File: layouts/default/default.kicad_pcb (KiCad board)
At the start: 2 copper layers, 38 x 75 mm, 43 parts, among them U2 LDO Vin max Iq, U3 LDO Vin max Iq

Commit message: Update layout
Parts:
- added C10: 100nF ±10% 16V X7R, atopile:C0402-b3ef17, B.Cu at (1.50, 15.2)
- added C11: 100nF ±10% 16V X7R, atopile:C0402-b3ef17, B.Cu at (1.50, 21.2)
- added C12: 100nF ±10% 16V X7R, atopile:C0402-b3ef17, B.Cu at (1.50, 27.2)
- added C17: , atopile:C_0402_1005Metric, B.Cu at (-0.95, 26.4)
- added C8: 100nF ±10% 16V X7R, atopile:C0402-b3ef17, B.Cu at (1.50, 3.00)
- added C9: 100nF ±10% 16V X7R, atopile:C0402-b3ef17, B.Cu at (1.50, 9.00)
- added S1: , atopile:KEY-SMD_4P-L4.2-W3.2-P2.20-LS4.6-a2ccf0, F.Cu at (7.07, 23.1)
- added S2: , atopile:KEY-SMD_4P-L4.2-W3.2-P2.20-LS4.6-a2ccf0, F.Cu at (7.07, 3.10)
- added XTAL1: , atopile:CRYSTAL-SMD_L3.2-W1.5-1-214bf9, F.Cu at (-11.0, 13.0)
- LED1, LED2, LED3, LED4, LED5, U7: moved to B.Cu
- moved U2 431.1 mm to (-21.0, -12.0)
- moved C7 277.4 mm to (2.50, 68.5), turned to 90 degrees
- moved X1 241.5 mm to (16.0, 12.0), turned to 90 degrees
- moved R1 205.2 mm to (-5.00, -13.0)
- moved R11 202.6 mm to (1.25, 68.5), turned to 90 degrees
- moved U7 176.7 mm to (16.2, 61.5)
- moved U3 174.1 mm to (-14.0, -12.0)
- moved R10 149.3 mm to (0.00, 68.5), turned to 90 degrees
- moved R9 109.6 mm to (-1.25, 68.5), turned to 90 degrees
- moved U1 42.4 mm to (3.00, 9.50)
- moved R2 37.5 mm to (3.00, -11.0)
- moved R5 22.0 mm to (-14.0, 16.0), turned to 90 degrees
- moved R7 16.5 mm to (13.0, 10.0)
- moved U8 14.0 mm to (-1.50, 19.0)
- moved J2 13.4 mm to (13.1, 21.8), turned to 180 degrees
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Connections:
- C1 pad 1: hv -> hv-2
- C1 pad 2: gnd-1 -> gnd
- C3 pad 1: hv-3 -> hv
- C3 pad 2: gnd-1 -> gnd
- C4 pad 2: gnd-1 -> gnd
- C5 pad 2: gnd-1 -> gnd
- C7 pad 2: gnd-1 -> gnd
- J1 pad 1: gnd-1 -> gnd
- J1 pad 10: line-9 -> line-4
- J1 pad 11: line-6 -> line-3
- J1 pad 13: usb_psu-hv -> hv-1
- J1 pad 14: gnd-1 -> gnd
- J1 pad 2: usb_psu-hv -> hv-1
- J1 pad 3: line-9 -> line-4
- J1 pad 4: line-6 -> line-3
- J1 pad 6: usb_psu-hv -> hv-1
- J1 pad 7: gnd-1 -> gnd
- J1 pad 8: gnd-1 -> gnd
- J1 pad 9: usb_psu-hv -> hv-1
- J2 pad 1: vindriktning_interface-line-1 -> vindriktning_interface-line
- J2 pad 2: vindriktning_interface-line -> vindriktning_interface-line-1
- J2 pad 3: hv-1 -> hv-3
- J2 pad 4: gnd-1 -> gnd
- LED1 pad 1: gnd-1 -> gnd
- LED1 pad 2: led_string-line-1 -> led_string-line-3
- LED1 pad 3: hv-1 -> hv-3
- LED2 pad 1: gnd-1 -> gnd
- LED2 pad 3: hv-1 -> hv-3
- LED2 pad 4: led_string-line-3 -> led_string-line-2
- LED3 pad 1: gnd-1 -> gnd
- LED3 pad 2: led_string-line-3 -> led_string-line-2
- LED3 pad 3: hv-1 -> hv-3
- LED4 pad 1: gnd-1 -> gnd
- LED4 pad 3: hv-1 -> hv-3
- LED4 pad 4: led_string-line-2 -> led_string-line-1
- LED5 pad 1: gnd-1 -> gnd
- LED5 pad 2: led_string-line-2 -> led_string-line-1
- LED5 pad 3: hv-1 -> hv-3
- Q1 pad 1: line -> line-6
- R1 pad 1: line-3 -> line-8
- R1 pad 2: hv -> hv-2
- R10 pad 2: gnd-1 -> gnd
- R11 pad 2: gnd-1 -> gnd
- R12 pad 1: line -> line-6
- R12 pad 2: gnd-1 -> gnd
- R2 pad 1: line-4 -> line-5
- R2 pad 2: hv -> hv-2
- R4 pad 2: hv-3 -> hv
- R6 pad 1: line-3 -> line-8
- R6 pad 2: hv-3 -> hv
- R7 pad 1: line-2 -> line-9
- R7 pad 2: hv-3 -> hv
- R9 pad 2: gnd-1 -> gnd
- U1 pad 10: line-4 -> line-5
- U1 pad 19: hv -> hv-2
- U1 pad 20: gnd-1 -> gnd
- U1 pad 21: gnd-1 -> gnd
- U1 pad 6: gnd-1 -> gnd
- U1 pad 7: hv -> hv-2
- U1 pad 9: line-3 -> line-8
- U2 pad 1: hv-1 -> hv-3
- U2 pad 2: gnd-1 -> gnd
- U2 pad 3: hv-1 -> hv-3
- U2 pad 5: hv-3 -> hv
- U3 pad 1: hv-1 -> hv-3
- U3 pad 2: gnd-1 -> gnd
- U3 pad 3: hv-1 -> hv-3
- U3 pad 5: hv -> hv-2
- U4 pad 1: hv -> hv-2
- U4 pad 3: gnd-1 -> gnd
- U4 pad 4: line-4 -> line-5
- U4 pad 6: line-3 -> line-8
- U5 pad 1: gnd-1 -> gnd
- U5 pad 11: gnd-1 -> gnd
- U5 pad 14: gnd-1 -> gnd
- U5 pad 16: mcu.mcu.esp32_c3_mini_1.ic-line-1 -> mcu.mcu.esp32_c3_mini_1.ic-line
- U5 pad 18: line -> line-6
- U5 pad 2: gnd-1 -> gnd
- U5 pad 20: line-8 -> line-10
- U5 pad 21: mcu.mcu.esp32_c3_mini_1.ic-line -> mcu.mcu.esp32_c3_mini_1.ic-line-1
- U5 pad 22: line-2 -> line-9
- U5 pad 26: line-9 -> line-4
- U5 pad 27: line-6 -> line-3
- U5 pad 3: hv-3 -> hv
- U5 pad 30: line-5 -> line
- U5 pad 31: line-10 -> line-2
- U5 pad 36: gnd-1 -> gnd
- U5 pad 37: gnd-1 -> gnd
- U5 pad 38: gnd-1 -> gnd
- U5 pad 39: gnd-1 -> gnd
- U5 pad 40: gnd-1 -> gnd
- U5 pad 41: gnd-1 -> gnd
- U5 pad 42: gnd-1 -> gnd
- U5 pad 43: gnd-1 -> gnd
- U5 pad 44: gnd-1 -> gnd
- U5 pad 45: gnd-1 -> gnd
- U5 pad 46: gnd-1 -> gnd
- U5 pad 47: gnd-1 -> gnd
- U5 pad 48: gnd-1 -> gnd
- U5 pad 49: gnd-1 -> gnd
- U5 pad 5: line-3 -> line-8
- U5 pad 50: gnd-1 -> gnd
- U5 pad 51: gnd-1 -> gnd
- U5 pad 52: gnd-1 -> gnd
- U5 pad 53: gnd-1 -> gnd
- U5 pad 54: gnd-1 -> gnd
- U5 pad 55: gnd-1 -> gnd
- U5 pad 56: gnd-1 -> gnd
- U5 pad 57: gnd-1 -> gnd
- U5 pad 58: gnd-1 -> gnd
- U5 pad 59: gnd-1 -> gnd
- U5 pad 6: line-4 -> line-5
- U5 pad 60: gnd-1 -> gnd
- U5 pad 61: gnd-1 -> gnd
- U6 pad 1: vindriktning_interface-line -> vindriktning_interface-line-1
- U6 pad 2: gnd-1 -> gnd
- U6 pad 3: hv -> hv-2
- U6 pad 5: line-2 -> line-9
- U6 pad 6: hv -> hv-2
- U6 pad 7: hv-1 -> hv-3
- U6 pad 8: vindriktning_interface-line-1 -> vindriktning_interface-line
- U7 pad 1: line-8 -> line-10
- U7 pad 2: line-10 -> line-2
- U7 pad 3: line-5 -> line
- U7 pad 4: gnd-1 -> gnd
- U7 pad 5: hv-1 -> hv-3
- U8 pad 2: gnd-1 -> gnd
- U8 pad 3: hv -> hv-2
- U8 pad 6: hv -> hv-2
- U8 pad 7: hv-1 -> hv-3
- U8 pad 8: led_string-line-1 -> led_string-line-3
- X1 pad 1: gnd -> gnd-1
- X1 pad 2: hv-2 -> hv-4
- X1 pad 3: line-4 -> line-5
- X1 pad 4: line-3 -> line-8
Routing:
- net (no net): track 0.00 -> 38.0 mm
- net gnd: track 0.00 -> 36.7 mm
- net hv-3: track 0.00 -> 31.4 mm, vias 0 -> 4
- net led_string-line-4: track 6.99 -> 38.0 mm
- net vindriktning_interface-line: track 0.00 -> 22.3 mm
- net vindriktning_interface-line-1: track 0.00 -> 18.7 mm
- net hv-4: track 0.00 -> 11.4 mm
- net mount[1]: track 0.00 -> 10.9 mm
- net led_string.leds[4]-line: track 0.00 -> 9.81 mm
- net co2_sensor.footprint.pins[19].net-net: track 0.00 -> 9.81 mm
- net cc1: track 0.00 -> 9.81 mm
- net mcu.mcu.low_speed_crystal_clock-net: track 0.00 -> 7.26 mm
- net mcu.mcu-line-1: track 0.00 -> 7.26 mm
- net led_string-line-1: track 2.77 -> 9.81 mm
- net led_string-line-3: track 6.99 -> 0.00 mm
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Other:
- board text added: "325bd98"

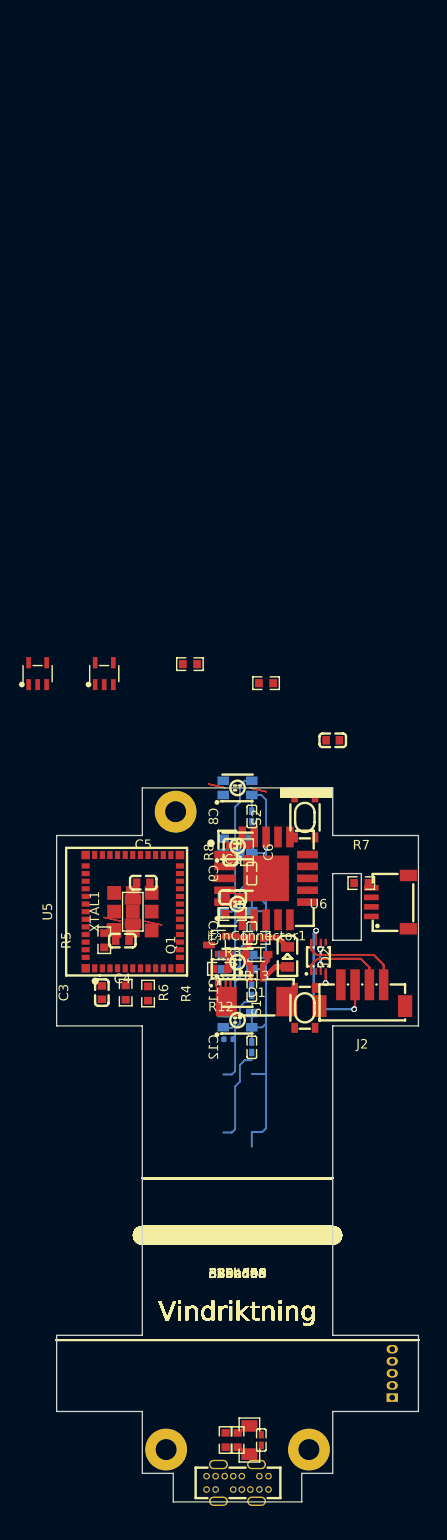
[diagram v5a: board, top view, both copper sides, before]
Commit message: Make it build with ato 0.8.x
- refactor modules
- clean up modules and structure
- convert some from fabll to ato
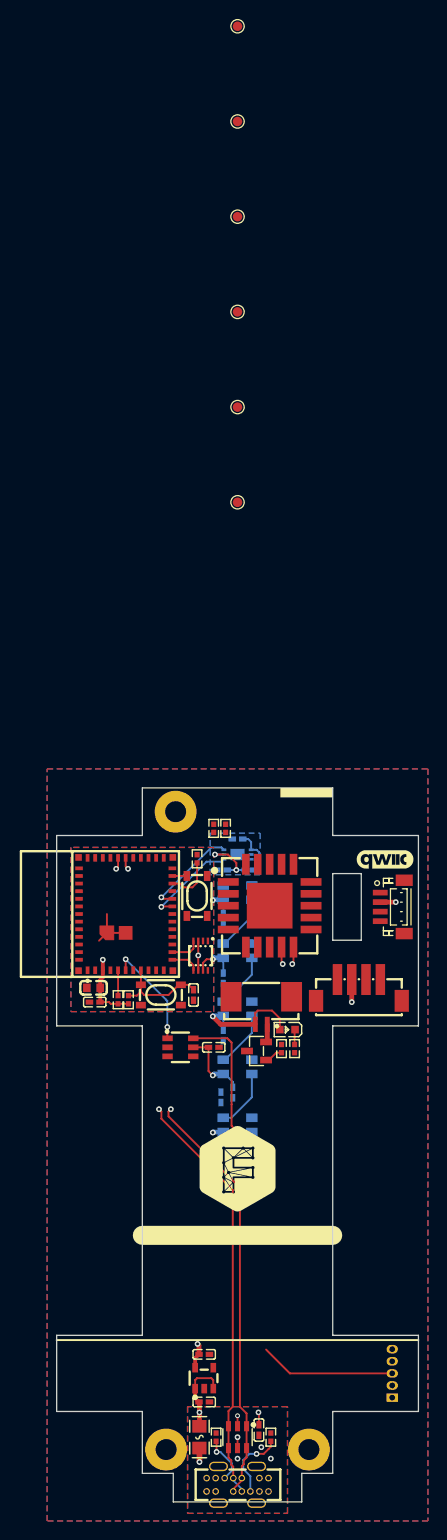
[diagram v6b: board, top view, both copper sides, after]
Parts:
- removed C17: , atopile:C_0402_1005Metric
- removed D1: 450mV, atopile:SOD-323_L1.8-W1.3-LS2.5-RD-b55baa
- removed D2: , atopile:LED0805-R-RD-d1137b
- removed J1: , atopile:USB-C-TH_TYPE-C-USB-14P-1a34cb
- removed R13, R7, R8: 10kΩ ±1% 100mW, atopile:R0603-ebcab9
- removed S1, S2: , atopile:KEY-SMD_4P-L4.2-W3.2-P2.20-LS4.6-a2ccf0
- removed XTAL1: , atopile:CRYSTAL-SMD_L3.2-W1.5-1-214bf9
- added C13: 100nF ±10% 16V X7R, atopile:C0402-b3ef17, B.Cu at (-1.62, 8.62)
- added C14: 100nF ±10% 16V X7R, atopile:C0402-b3ef17, F.Cu at (2.25, 67.5)
- added CN1: , atopile:CONN-SMD_BM04B-SRSS-TB-6963ef, F.Cu at (16.2, 12.5)
- added LOGO1: , lib:faebrykLogo_8x9mm, F.Cu at (0.00, 40.0)
- added TP1: , TestPoint:TestPoint_Pad_D1.0mm, F.Cu at (0.00, -70.0)
- added TP2: , TestPoint:TestPoint_Pad_D1.0mm, F.Cu at (0.00, -30.0)
- added TP3: , TestPoint:TestPoint_Pad_D1.0mm, F.Cu at (0.00, -50.0)
- added TP4: , TestPoint:TestPoint_Pad_D1.0mm, F.Cu at (0.00, -80.0)
- added TP5: , TestPoint:TestPoint_Pad_D1.0mm, F.Cu at (0.00, -40.0)
- added TP6: , TestPoint:TestPoint_Pad_D1.0mm, F.Cu at (0.00, -60.0)
- added U10: , atopile:VSON8_L2.0-W2.3-P0.50-LS3.1-BL-9e6526, F.Cu at (-3.88, 17.6)
- added U11: 2V, lib:LED0603-RD, F.Cu at (5.25, 25.4)
- added U12: , atopile:SOT-23-6_L2.9-W1.6-P0.95-LS2.8-BL-d2c740, F.Cu at (0.00, 68.2)
- added U13: , atopile:F0805-d5954a, F.Cu at (-4.00, 68.2)
- added U9: , lib:qwiic_6mm, F.Cu at (15.5, 7.50)
- C1, C2: value 100nF ±10% 50V X7R -> 100nF ±10% 16V X7R; footprint atopile:C0603-bd72f6 -> atopile:C0402-b3ef17
- C10: value 100nF ±10% 16V X7R -> 22µF ±20% 6.3V X5R; footprint atopile:C0402-b3ef17 -> atopile:C0603-bd72f6; moved to F.Cu
- C11: moved to F.Cu
- C12: value 100nF ±10% 16V X7R -> 1µF ±10% 16V X5R; moved to F.Cu
- C3: value 1µF ±10% 50V X5R -> 100nF ±10% 16V X7R; footprint atopile:C0603-bd72f6 -> atopile:C0402-b3ef17
- C4, C5, C6: value 100nF ±10% 50V X7R -> 100nF ±10% 16V X7R; footprint atopile:C0603-bd72f6 -> atopile:C0402-b3ef17; moved to B.Cu
- C7: value 100nF ±5% 16V X7R -> 100nF ±10% 16V X7R; moved to B.Cu
- Q1: footprint atopile:SOT-23-3_L2.9-W1.3-P1.90-LS2.4-BL-1-fcaf94 -> atopile:SOT-23-3_L2.9-W1.3-P1.90-LS2.4-BR-688f29
- R1: value 10kΩ ±1% 100mW -> 1kΩ ±1% 62.5mW; footprint atopile:R0603-ebcab9 -> atopile:R0402-56259e; moved to B.Cu
- R10: value 5.1kΩ ±1% 100mW -> 1kΩ ±1% 62.5mW; footprint atopile:R0603-ebcab9 -> atopile:R0402-56259e
- R11: value 1MΩ ±1% 250mW -> 10kΩ ±1% 62.5mW; footprint atopile:R1206-bdb864 -> atopile:R0402-56259e
- R12, R3, R4, R5: value 10kΩ ±1% 100mW -> 10kΩ ±1% 62.5mW; footprint atopile:R0603-ebcab9 -> atopile:R0402-56259e
- R2, R6: value 10kΩ ±1% 100mW -> 5.1kΩ ±1% 62.5mW; footprint atopile:R0603-ebcab9 -> atopile:R0402-56259e
- R9: value 5.1kΩ ±1% 100mW -> 10kΩ ±1% 62.5mW; footprint atopile:R0603-ebcab9 -> atopile:R0402-56259e
- U2: value LDO Vin max Iq -> LDO 3.3V ±0% 850.5mA 320mV Vin max Iq 10µA; footprint atopile:SOT-23-5_L3.0-W1.7-P0.95-LS2.8-BL-01dfeb -> atopile:SOT-23-5_L2.9-W1.6-P0.95-LS2.8-BR-2dcca4
- U3: value LDO Vin max Iq -> (none); footprint atopile:SOT-23-5_L3.0-W1.7-P0.95-LS2.8-BL-01dfeb -> atopile:SOT-23-6_L2.9-W1.6-P0.95-LS2.8-BR-bfc73b
- U5: footprint atopile:WIFIM-SMD_ESP32-C3-MINI-MINI-1U-1cb675 -> lib:KEY-SMD_4P-L4.2-W3.2-P2.20-LS4.6
- U6: footprint atopile:VSON8_L2.0-W2.3-P0.50-LS3.1-BL-9e6526 -> atopile:WIFIM-SMD_ESP32-C3-MINI-1-fcb454
- U7: footprint atopile:SENSORM-TH_HLK-LD2410B-P-2a325e -> lib:KEY-SMD_4P-L4.2-W3.2-P2.20-LS4.6; moved to F.Cu
- U8: footprint atopile:VSON8_L2.0-W2.3-P0.50-LS3.1-BL-9e6526 -> atopile:SENSORM-TH_HLK-LD2410B-P-2a325e; moved to B.Cu
- X1: footprint atopile:CONN-SMD_4P-P1.00_SM04B-SRSS-TB-LF-SN-d36980 -> atopile:USB-C-TH_TYPE-C-USB-14P-1a34cb
- moved R2 79.4 mm to (-2.25, 68.2), turned to 90 degrees
- moved U2 76.0 mm to (-3.50, 62.0), turned to -90 degrees
- moved C1 70.8 mm to (-3.50, 64.5)
- moved R11 64.3 mm to (-1.25, 4.25)
- moved X1 63.3 mm to (0.00, 73.2), turned to 0 degrees
- moved R6 49.1 mm to (3.50, 68.2), turned to 90 degrees
- moved C7 48.7 mm to (-1.50, 20.0), turned to -90 degrees
- moved C2 48.1 mm to (-3.50, 59.5)
- moved U7 46.6 mm to (-8.05, 21.8), turned to 180 degrees
- moved U8 46.1 mm to (16.2, 61.5)
- moved R10 41.5 mm to (6.00, 27.4), turned to -90 degrees
- moved R9 41.5 mm to (4.62, 27.4)
- moved U3 40.1 mm to (-6.00, 27.2), turned to 180 degrees
- moved LED1 35.4 mm to (0.00, 35.4), turned to 0 degrees
- moved C5 24.0 mm to (-0.50, 32.0), turned to -90 degrees
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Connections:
- net ldo_mcu.footprint.pins[3].net-net renamed ldo.ldo.footprint.pins[3].net-net
- net ldo_peripheral.footprint.pins[3].net-net renamed led_buffer-line-1
- net led_string-line renamed line-19
- net led_string-line-2 renamed line-13
- C10 pad 1: hv-3 -> hv
- C11 pad 1: hv-3 -> hv
- C12 pad 1: hv-3 -> output
- C2 pad 1: mcu.mcu.boot_switch.lp_filter-line -> hv
- C2 pad 2: mcu.mcu.boot_switch.lp_filter-gnd -> gnd
- C3 pad 1: hv -> hv-2
- C4 pad 1: mcu.mcu.low_speed_crystal_clock-net -> hv-2
- C5 pad 1: mcu.mcu-line-1 -> hv-2
- C6 pad 1: mcu.mcu.reset_switch.lp_filter-line -> hv-2
- C6 pad 2: mcu.mcu.reset_switch.lp_filter-gnd -> gnd
- C7 pad 1: shield -> hv-2
- C8 pad 1: hv-3 -> hv-2
- C9 pad 1: hv-3 -> hv
- FanConnector1 pad 1: vindriktning_interface.fan_controller-gnd-1 -> vindriktning_interface.fan_controller-gnd
- FanConnector1 pad 2: vindriktning_interface.fan_controller-hv -> hv-2
- H1 pad 1: (no net) -> pcb_mount.screw_holes[0]-contact
- H2 pad 1: (no net) -> pcb_mount.screw_holes[1]-contact
- H3 pad 1: (no net) -> pcb_mount.screw_holes[2]-contact
- J2 pad 1: vindriktning_interface-line -> pin[0]
- J2 pad 2: vindriktning_interface-line-1 -> pin[1]
- J2 pad 3: hv-3 -> hv-2
- LED1 pad 2: led_string-line-3 -> line-21
- LED1 pad 3: hv-3 -> hv-2
- LED2 pad 3: hv-3 -> hv-2
- LED3 pad 3: hv-3 -> hv-2
- LED3 pad 4: led_string-line-4 -> line-3
- LED4 pad 2: led_string-line-4 -> line-3
- LED4 pad 3: hv-3 -> hv-2
- LED4 pad 4: led_string-line-1 -> line-2
- LED5 pad 2: led_string-line-1 -> line-2
- LED5 pad 3: hv-3 -> hv-2
- LED5 pad 4: led_string.leds[4]-line -> line
- Q1 pad 1: line-6 -> line-16
- Q1 pad 2: vindriktning_interface.fan_controller-gnd-1 -> vindriktning_interface.fan_controller-gnd
- Q1 pad 3: vindriktning_interface.fan_controller-gnd -> gnd
- R1 pad 1: line-8 -> hv
- R1 pad 2: hv-2 -> DVI
- R10 pad 1: cc2 -> cathode
- R10 pad 2: gnd -> vindriktning_interface.fan_controller-gnd
- R11 pad 1: shield -> line-5
- R11 pad 2: gnd -> hv
- R12 pad 2: gnd -> hv
- R2 pad 1: line-5 -> line-12
- R2 pad 2: hv-2 -> gnd
- R3 pad 1: mcu.mcu.boot_switch-line -> line-4
- R3 pad 2: mcu.mcu.boot_switch.lp_filter-line -> hv
- R4 pad 1: mcu.mcu-line -> line-14
- R5 pad 1: mcu.mcu.low_speed_crystal_clock-net -> hv
- R5 pad 2: mcu.mcu-line-2 -> output
- R6 pad 1: line-8 -> line-15
- R6 pad 2: hv -> gnd
- R9 pad 1: cc1 -> line-16
- U1 pad 10: line-5 -> line-6
- U1 pad 19: hv-2 -> hv
- U1 pad 7: hv-2 -> hv
- U1 pad 9: line-8 -> line-5
- U2 pad 1: hv-3 -> hv-2
- U2 pad 3: hv-3 -> hv-2
- U3 pad 1: hv-3 -> line-7
- U3 pad 3: hv-3 -> led_buffer-line
- U4 pad 1: hv-2 -> hv
- U4 pad 2: lux_sensor.ic-line-1 -> gnd
- U4 pad 4: line-5 -> line-6
- U4 pad 5: lux_sensor.ic-line -> DVI
- U4 pad 6: line-8 -> line-5
- U4 pad 7: lux_sensor.ic-line-2 -> gnd
- U5 pad 3: hv -> output-1
- U5 pad 4: mcu.mcu.esp32_c3_mini_1.ic.footprint.pins[33].net-net -> output-1
- U6 pad 1: vindriktning_interface-line-1 -> gnd
- U6 pad 3: hv-2 -> hv
- U6 pad 4: line-1 -> mcu.ic.footprint.pins[33].net-net
- U6 pad 5: line-9 -> line-4
- U6 pad 6: hv-2 -> line-7
- U6 pad 7: hv-3 -> mcu.ic.footprint.pins[50].net-net
- U6 pad 8: vindriktning_interface-line -> output
- U7 pad 1: line-10 -> gnd
- U7 pad 2: line-2 -> gnd
- U7 pad 3: line -> output
- U7 pad 4: gnd -> output
- U8 pad 1: led_string.runtime_anon[0]-line-1 -> line-10
- U8 pad 2: gnd -> line-18
- U8 pad 3: hv-2 -> line-20
- U8 pad 4: led_string.runtime_anon[0]-line -> gnd
- U8 pad 5: line-7 -> hv-2
- X1 pad 1: gnd-1 -> gnd
- X1 pad 2: hv-4 -> hv-1
- X1 pad 3: line-5 -> line-17
- X1 pad 4: line-8 -> line-1
- X1 pad 5: qwiic_connector.footprint.pins[4].net-net -> line-15
- X1 pad 6: qwiic_connector.footprint.pins[5].net-net -> hv-1
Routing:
- net line-17: track 0.00 -> 44.2 mm, vias 0 -> 1
- net line-1: track 2.41 -> 44.1 mm, vias 2 -> 1
- net led_string-line-4: track 38.0 -> 0.00 mm
- net (no net): track 38.0 -> 0.00 mm
- net hv-2: track 6.28 -> 41.9 mm, vias 4 -> 9
- net hv-3: track 31.4 -> 0.00 mm, vias 4 -> 0
- net gnd: track 36.7 -> 7.86 mm, vias 0 -> 4
- net vindriktning_interface-line: track 22.3 -> 0.00 mm
- net hv: track 0.00 -> 20.4 mm, vias 0 -> 4
- net vindriktning_interface-line-1: track 18.7 -> 0.00 mm
- net line-20: track 0.00 -> 15.5 mm, vias 0 -> 1
- net line-21: track 0.00 -> 15.4 mm, vias 0 -> 1
- net vindriktning_interface.fan_controller-gnd-1: track 13.1 -> 0.00 mm
- net line-5: track 0.00 -> 11.9 mm, vias 0 -> 2
- net hv-4: track 11.4 -> 0.00 mm
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- added copper zone on B.Cu, net (none)
- added copper zone on F.Cu, net (none)
- added copper zone on B.Cu, net gnd
- added copper zone on F.Cu, net gnd
- added copper zone on In1.Cu, net gnd
- added copper zone on In2.Cu, net hv
- added copper zone on In2.Cu, net hv-1
- added copper zone on In2.Cu, net hv-2
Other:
- copper layers 2 -> 4
- board text removed: "069b639"
- board text removed: "325bd98"
- board text removed: "380a7ca"
- board text removed: "Vindriktning"
- board text removed: "a4eeddd"
- board text removed: "d9546bd"

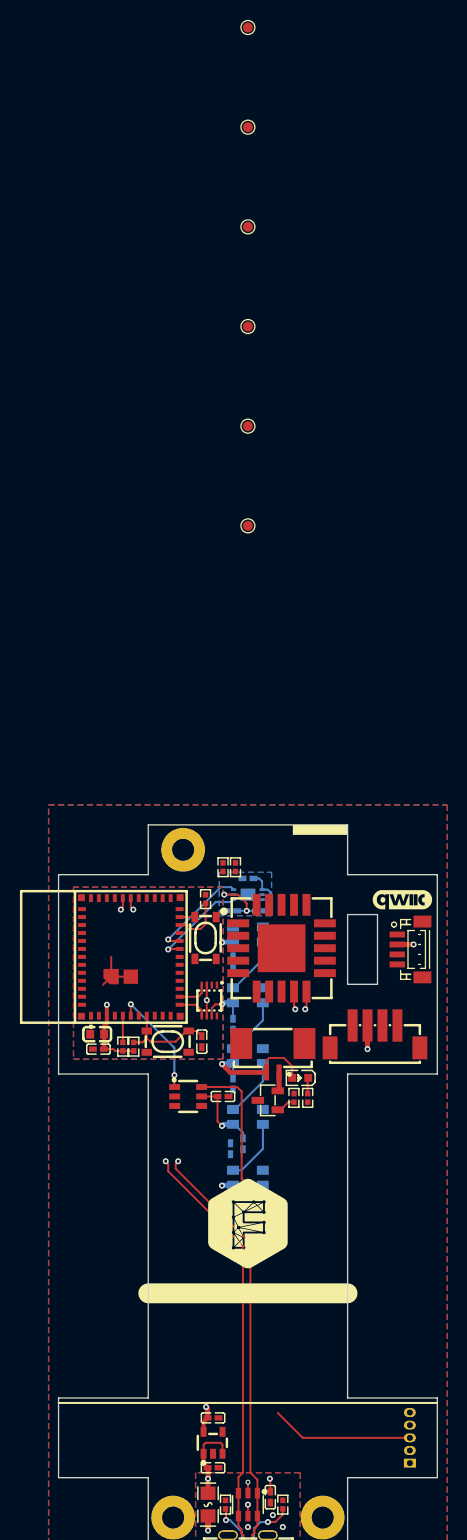
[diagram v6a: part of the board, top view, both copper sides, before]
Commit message: Finish layout, swap to ufl version of esp32c3
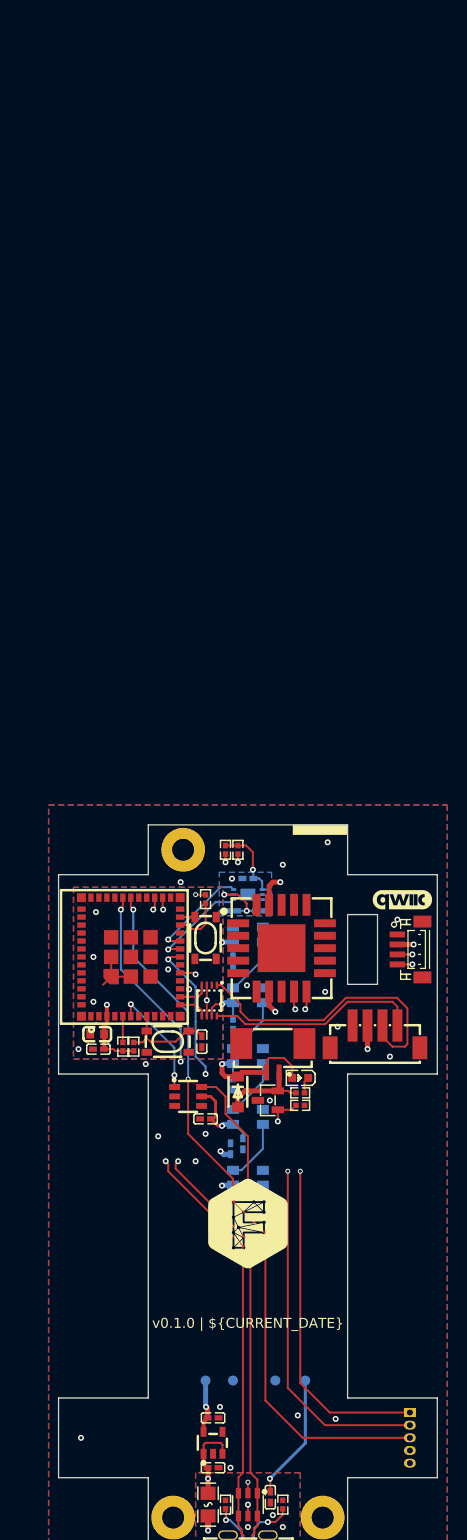
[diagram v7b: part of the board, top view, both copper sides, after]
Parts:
- removed TP5, TP6: , TestPoint:TestPoint_Pad_D1.0mm
- added D1: , atopile:SOD-123F_L2.8-W1.8-LS3.7-RD-7788aa, F.Cu at (-1.00, 26.8)
- C12: value 1µF ±10% 16V X5R -> 1µF ±10% 25V X5R
- TP1, TP2, TP3, TP4: moved to B.Cu
- U6: footprint atopile:WIFIM-SMD_ESP32-C3-MINI-1-fcb454 -> atopile:WIFIM-SMD_ESP32-C3-MINI-MINI-1U-1cb675
- U8: moved to F.Cu
- moved TP4 135.8 mm to (-1.50, 55.8)
- moved TP1 125.8 mm to (-4.25, 55.8)
- moved TP3 105.9 mm to (5.75, 55.8)
- moved TP2 85.8 mm to (2.75, 55.8)
- moved C3 2.85 mm to (-4.25, 29.5), turned to 180 degrees
- moved R11 1.77 mm to (-1.00, 2.50)
- moved R12 1.77 mm to (-2.25, 2.50)
- moved R9 0.98 mm to (5.25, 28.1), turned to 0 degrees
- moved R10 0.90 mm to (5.25, 26.9), turned to 180 degrees
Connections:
- net mcu.ic.footprint.pins[50].net-net renamed mcu.ic.footprint.pins[58].net-net
- net mcu.ic.footprint.pins[52].net-net renamed mcu.ic.footprint.pins[60].net-net
- C1 pad 1: hv-2 -> hv
- C10 pad 1: hv -> hv-1
- C11 pad 1: hv -> hv-1
- C14 pad 1: hv-2 -> hv
- C2 pad 1: hv -> hv-1
- C3 pad 1: hv-2 -> hv
- C4 pad 1: hv-2 -> hv
- C5 pad 1: hv-2 -> hv
- C6 pad 1: hv-2 -> hv
- C7 pad 1: hv-2 -> hv
- C8 pad 1: hv-2 -> hv
- C9 pad 1: hv -> hv-1
- CN1 pad 2: hv -> hv-1
- CN1 pad 3: line-6 -> line-8
- CN1 pad 4: line-5 -> line-1
- FanConnector1 pad 2: hv-2 -> hv
- J2 pad 3: hv-2 -> hv
- LED1 pad 2: line-21 -> line-17
- LED1 pad 3: hv-2 -> hv
- LED1 pad 4: line-19 -> line
- LED2 pad 2: line-19 -> line
- LED2 pad 3: hv-2 -> hv
- LED2 pad 4: line-13 -> line-10
- LED3 pad 2: line-13 -> line-10
- LED3 pad 3: hv-2 -> hv
- LED3 pad 4: line-3 -> line-19
- LED4 pad 2: line-3 -> line-19
- LED4 pad 3: hv-2 -> hv
- LED5 pad 3: hv-2 -> hv
- LED5 pad 4: line -> line-5
- Q1 pad 1: line-16 -> line-3
- R1 pad 1: hv -> hv-1
- R11 pad 1: line-5 -> line-1
- R11 pad 2: hv -> hv-1
- R12 pad 1: line-6 -> line-8
- R12 pad 2: hv -> hv-1
- R2 pad 1: line-12 -> line-16
- R3 pad 1: line-4 -> line-11
- R3 pad 2: hv -> hv-1
- R4 pad 1: line-14 -> line-4
- R4 pad 2: hv -> hv-1
- R5 pad 1: hv -> hv-1
- R6 pad 1: line-15 -> line-21
- R9 pad 1: line-16 -> line-3
- TP1 pad 1: tp_3v3[0]-contact -> hv-1
- TP2 pad 1: tp_3v3[1]-contact -> gnd
- TP3 pad 1: tp_5v[0]-contact -> hv
- TP4 pad 1: tp_5v[1]-contact -> gnd
- U1 pad 10: line-6 -> line-8
- U1 pad 19: hv -> hv-1
- U1 pad 7: hv -> hv-1
- U1 pad 9: line-5 -> line-1
- U10 pad 3: hv -> hv-1
- U10 pad 4: line-8 -> line-9
- U10 pad 5: line-9 -> line-6
- U10 pad 6: hv -> hv-1
- U10 pad 7: hv-2 -> hv
- U11 pad 2: hv-2 -> hv
- U12 pad 1: line-17 -> line-15
- U12 pad 3: line-1 -> line-12
- U12 pad 4: line-1 -> line-12
- U12 pad 5: hv-2 -> hv
- U12 pad 6: line-17 -> line-15
- U13 pad 1: hv-1 -> hv-2
- U13 pad 2: hv-2 -> hv
- U2 pad 1: hv-2 -> hv
- U2 pad 3: hv-2 -> hv
- U2 pad 5: hv -> hv-1
- U3 pad 1: line-7 -> line-14
- U3 pad 5: hv-2 -> hv
- U3 pad 6: line-21 -> line-17
- U4 pad 1: hv -> hv-1
- U4 pad 4: line-6 -> line-8
- U4 pad 6: line-5 -> line-1
- U6 pad 12: line-9 -> line-6
- U6 pad 13: line-8 -> line-9
- U6 pad 16: line-10 -> line-13
- U6 pad 18: line-16 -> line-3
- U6 pad 19: line-6 -> line-8
- U6 pad 20: line-5 -> line-1
- U6 pad 21: line-11 -> line-18
- U6 pad 22: line-14 -> line-4
- U6 pad 26: line-17 -> line-15
- U6 pad 27: line-1 -> line-12
- U6 pad 3: hv -> hv-1
- U6 pad 31: line-18 -> line-7
- U6 pad 5: line-4 -> line-11
- U6 pad 6: line-7 -> line-14
- U8 pad 1: line-10 -> line-13
- U8 pad 2: line-18 -> line-7
- U8 pad 5: hv-2 -> hv
- X1 pad 10: line-17 -> line-15
- X1 pad 11: line-1 -> line-12
- X1 pad 12: line-12 -> line-16
- X1 pad 13: hv-1 -> hv-2
- X1 pad 2: hv-1 -> hv-2
- X1 pad 3: line-17 -> line-15
- X1 pad 4: line-1 -> line-12
- X1 pad 5: line-15 -> line-21
- X1 pad 6: hv-1 -> hv-2
- X1 pad 9: hv-1 -> hv-2
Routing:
- net line-12: track 5.10 -> 71.5 mm, vias 1 -> 2
- net line-15: track 7.66 -> 71.7 mm, vias 1 -> 2
- net line-8: track 3.18 -> 67.0 mm, vias 0 -> 4
- net line-7: track 11.3 -> 70.0 mm, vias 2 -> 3
- net line-20: track 15.5 -> 72.0 mm, vias 1 -> 2
- net line-13: track 5.96 -> 61.0 mm, vias 0 -> 2
- net hv-2: track 41.9 -> 1.46 mm, vias 9 -> 1
- net hv: track 20.4 -> 55.6 mm, vias 4 -> 10
- net hv-1: track 1.46 -> 35.2 mm, vias 1 -> 8
- net line-17: track 44.2 -> 14.1 mm
- net pin[1]: track 0.00 -> 30.1 mm
- net pin[0]: track 0.00 -> 21.5 mm
- net line-3: track 5.95 -> 26.7 mm, vias 0 -> 3
- net line-1: track 44.1 -> 64.5 mm, vias 1 -> 4
- net line-5: track 11.9 -> 0.00 mm, vias 2 -> 0
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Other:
- board text added: "3V3"
- board text added: "5V"
- board text added: "GND"
- board text added: "v0.1.0 | ${CURRENT_DATE}"
